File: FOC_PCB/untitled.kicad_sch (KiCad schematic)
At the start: 16 parts, among them SW2 SW_Push, U1 STM32G491RET6, X1 OXETDLJANF-8MHZ

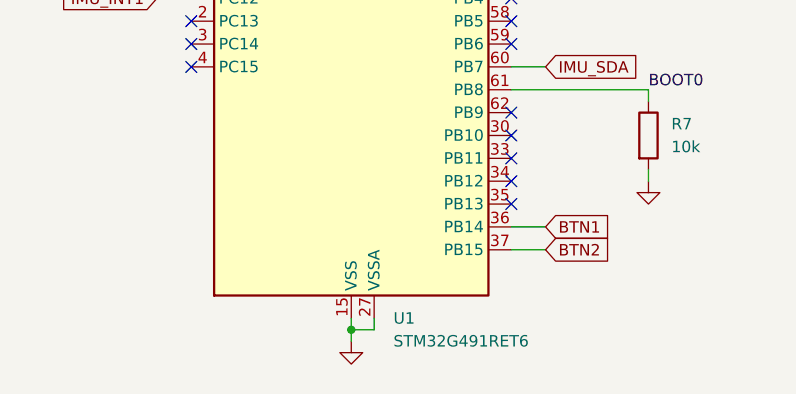
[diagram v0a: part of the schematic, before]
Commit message: Add net class colors
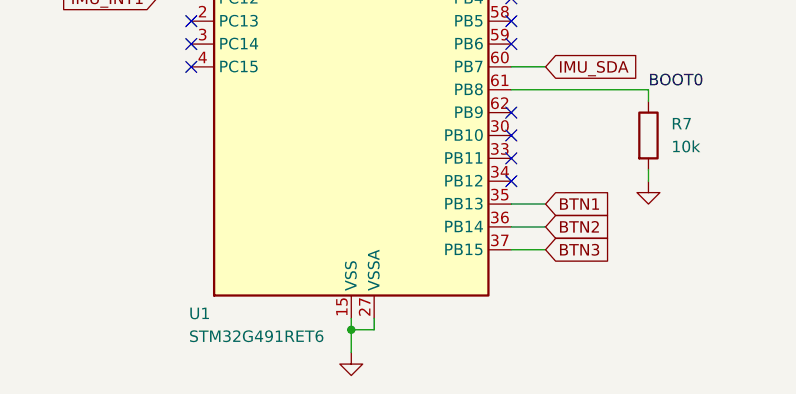
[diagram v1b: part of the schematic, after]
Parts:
- C10, C11, C12, C13, C14, C2, C20, C21, C22, C23, C8: footprint Capacitor_SMD:C_0603_1608Metric -> Capacitor_SMD:C_0603_1608Metric_Pad1.08x0.95mm_HandSolder
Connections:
- net BTN1: now also U1.35 (PB13); no longer U1.36 (PB14)
- net BTN2: now also U1.36 (PB14); no longer U1.37 (PB15)
- new net BTN3: U1.37 (PB15)
- no-connect marks 25 -> 24
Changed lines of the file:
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@@
 	)
 	(no_connect
-		(at 163.83 148.59)
-	)
-	(no_connect
 		(at 163.83 72.39)
 	)
@@
 	(wire
 		(pts
-			(xy 146.05 162.56) (xy 146.05 163.83)
+			(xy 146.05 162.56) (xy 146.05 165.1)
 		)
 		(stroke
@@
 	(wire
 		(pts
-			(xy 163.83 153.67) (xy 167.64 153.67)
-		)
-		(stroke
-			(width 0)
-			(type default)
-		)
-	)
-	(wire
-		(pts
 			(xy 149.86 27.94) (xy 166.37 27.94)
 		)
@@
 	(wire
 		(pts
-			(xy 163.83 151.13) (xy 167.64 151.13)
-		)
-		(stroke
-			(width 0)
-			(type default)
-		)
-	)
-	(wire
-		(pts
 			(xy 102.87 41.91) (xy 114.3 41.91)
 		)
@@
 	(wire
 		(pts
+			(xy 163.83 148.59) (xy 167.64 148.59)
+		)
+		(stroke
+			(width 0)
+			(type default)
+		)
+	)
+	(wire
+		(pts
 			(xy 163.83 74.93) (xy 167.64 74.93)
 		)
@@
 	(wire
 		(pts
+			(xy 163.83 153.67) (xy 167.64 153.67)
+		)
+		(stroke
+			(width 0)
+			(type default)
+		)
+	)
+	(wire
+		(pts
 			(xy 179.07 137.16) (xy 179.07 135.89)
 		)
@@
 	(wire
 		(pts
+			(xy 163.83 151.13) (xy 167.64 151.13)
+		)
+		(stroke
+			(width 0)
+			(type default)
+		)
+	)
+	(wire
+		(pts
 			(xy 189.23 39.37) (xy 189.23 41.91)
 		)
@@
 	(global_label "BTN1"
 		(shape input)
-		(at 167.64 151.13 0)
+		(at 167.64 148.59 0)
 		(fields_autoplaced yes)
 		(effects
@@
 		)
 		(property "Intersheetrefs" "${INTERSHEET_REFS}"
-			(at 175.4028 151.13 0)
+			(at 175.4028 148.59 0)
 			(hide yes)
 			(show_name no)
@@
 	(global_label "BTN2"
 		(shape input)
-		(at 167.64 153.67 0)
+		(at 167.64 151.13 0)
 		(fields_autoplaced yes)
 		(effects
@@
 		)
 		(property "Intersheetrefs" "${INTERSHEET_REFS}"
-			(at 175.4028 153.67 0)
+			(at 175.4028 151.13 0)
 			(hide yes)
 			(show_name no)
@@
 		)
 	)
+	(global_label "BTN3"
+		(shape input)
+		(at 167.64 153.67 0)
+		(fields_autoplaced yes)
+		(effects
+			(font
+				(size 1.27 1.27)
+			)
+			(justify left)
+		)
+		(property "Intersheetrefs" "${INTERSHEET_REFS}"
+			(at 175.4028 153.67 0)
+			(hide yes)
+			(show_name no)
+			(do_not_autoplace no)
+			(effects
+				(font
+					(size 1.27 1.27)
+				)
+				(justify left)
+			)
+		)
+	)
 	(global_label "T_CS"
 		(shape input)
@@
 		(in_pos_files yes)
 		(dnp no)
-		(fields_autoplaced yes)
 		(property "Reference" "U1"
-			(at 150.7333 161.29 0)
+			(at 128.016 160.782 0)
 			(show_name no)
 			(do_not_autoplace no)
@@
 		)
 		(property "Value" "STM32G491RET6"
-			(at 150.7333 163.83 0)
+			(at 128.016 163.322 0)
 			(show_name no)
 			(do_not_autoplace no)
@@
 			)
 		)
-		(property "Footprint" "Capacitor_SMD:C_0603_1608Metric"
+		(property "Footprint" "Capacitor_SMD:C_0603_1608Metric_Pad1.08x0.95mm_HandSolder"
 			(at 113.3348 39.37 0)
 			(hide yes)
@@
 			)
 		)
-		(property "Footprint" "Capacitor_SMD:C_0603_1608Metric"
+		(property "Footprint" "Capacitor_SMD:C_0603_1608Metric_Pad1.08x0.95mm_HandSolder"
 			(at 89.2048 39.37 0)
 			(hide yes)
@@
 			)
 		)
-		(property "Footprint" "Capacitor_SMD:C_0603_1608Metric"
+		(property "Footprint" "Capacitor_SMD:C_0603_1608Metric_Pad1.08x0.95mm_HandSolder"
 			(at 79.0448 82.55 0)
 			(hide yes)
@@
 			)
 		)
-		(property "Footprint" "Capacitor_SMD:C_0603_1608Metric"
+		(property "Footprint" "Capacitor_SMD:C_0603_1608Metric_Pad1.08x0.95mm_HandSolder"
 			(at 176.8348 39.37 0)
 			(hide yes)
@@
 			)
 		)
-		(property "Footprint" "Capacitor_SMD:C_0603_1608Metric"
+		(property "Footprint" "Capacitor_SMD:C_0603_1608Metric_Pad1.08x0.95mm_HandSolder"
 			(at 66.3448 118.11 0)
 			(hide yes)
@@
 			)
 		)
-		(property "Footprint" "Capacitor_SMD:C_0603_1608Metric"
+		(property "Footprint" "Capacitor_SMD:C_0603_1608Metric_Pad1.08x0.95mm_HandSolder"
 			(at 101.9048 39.37 0)
 			(hide yes)
@@
 			)
 		)
-		(property "Footprint" "Capacitor_SMD:C_0603_1608Metric"
+		(property "Footprint" "Capacitor_SMD:C_0603_1608Metric_Pad1.08x0.95mm_HandSolder"
 			(at 124.7648 39.37 0)
 			(hide yes)
@@
 			)
 		)
-		(property "Footprint" "Capacitor_SMD:C_0603_1608Metric"
+		(property "Footprint" "Capacitor_SMD:C_0603_1608Metric_Pad1.08x0.95mm_HandSolder"
 			(at 137.4648 39.37 0)
 			(hide yes)
@@
 	(symbol
 		(lib_id "power:GNDA")
-		(at 146.05 163.83 0)
+		(at 146.05 165.1 0)
 		(unit 1)
 		(body_style 1)
@@
 		(fields_autoplaced yes)
 		(property "Reference" "#PWR055"
-			(at 146.05 170.18 0)
+			(at 146.05 171.45 0)
 			(hide yes)
 			(show_name no)
@@
 		)
 		(property "Value" "GNDA"
-			(at 146.05 168.91 0)
+			(at 146.05 170.18 0)
 			(hide yes)
 			(show_name no)
@@
 		)
 		(property "Footprint" ""
-			(at 146.05 163.83 0)
+			(at 146.05 165.1 0)
 			(hide yes)
 			(show_name no)
@@
 		)
 		(property "Datasheet" ""
-			(at 146.05 163.83 0)
+			(at 146.05 165.1 0)
 			(hide yes)
 			(show_name no)
@@
 		)
 		(property "Description" "Power symbol creates a global label with name \"GNDA\" , analog ground"
-			(at 146.05 163.83 0)
+			(at 146.05 165.1 0)
 			(hide yes)
 			(show_name no)
@@
 			)
 		)
-		(property "Footprint" "Capacitor_SMD:C_0603_1608Metric"
+		(property "Footprint" "Capacitor_SMD:C_0603_1608Metric_Pad1.08x0.95mm_HandSolder"
 			(at 165.4048 39.37 0)
 			(hide yes)
@@
 			)
 		)
-		(property "Footprint" "Capacitor_SMD:C_0603_1608Metric"
+		(property "Footprint" "Capacitor_SMD:C_0603_1608Metric_Pad1.08x0.95mm_HandSolder"
 			(at 188.2648 39.37 0)
 			(hide yes)
@@
 			)
 		)
-		(property "Footprint" "Capacitor_SMD:C_0603_1608Metric"
+		(property "Footprint" "Capacitor_SMD:C_0603_1608Metric_Pad1.08x0.95mm_HandSolder"
 			(at 153.9748 39.37 0)
 			(hide yes)
